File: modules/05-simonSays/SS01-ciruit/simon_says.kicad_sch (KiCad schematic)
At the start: 18 parts, among them J1 MODULE Connector

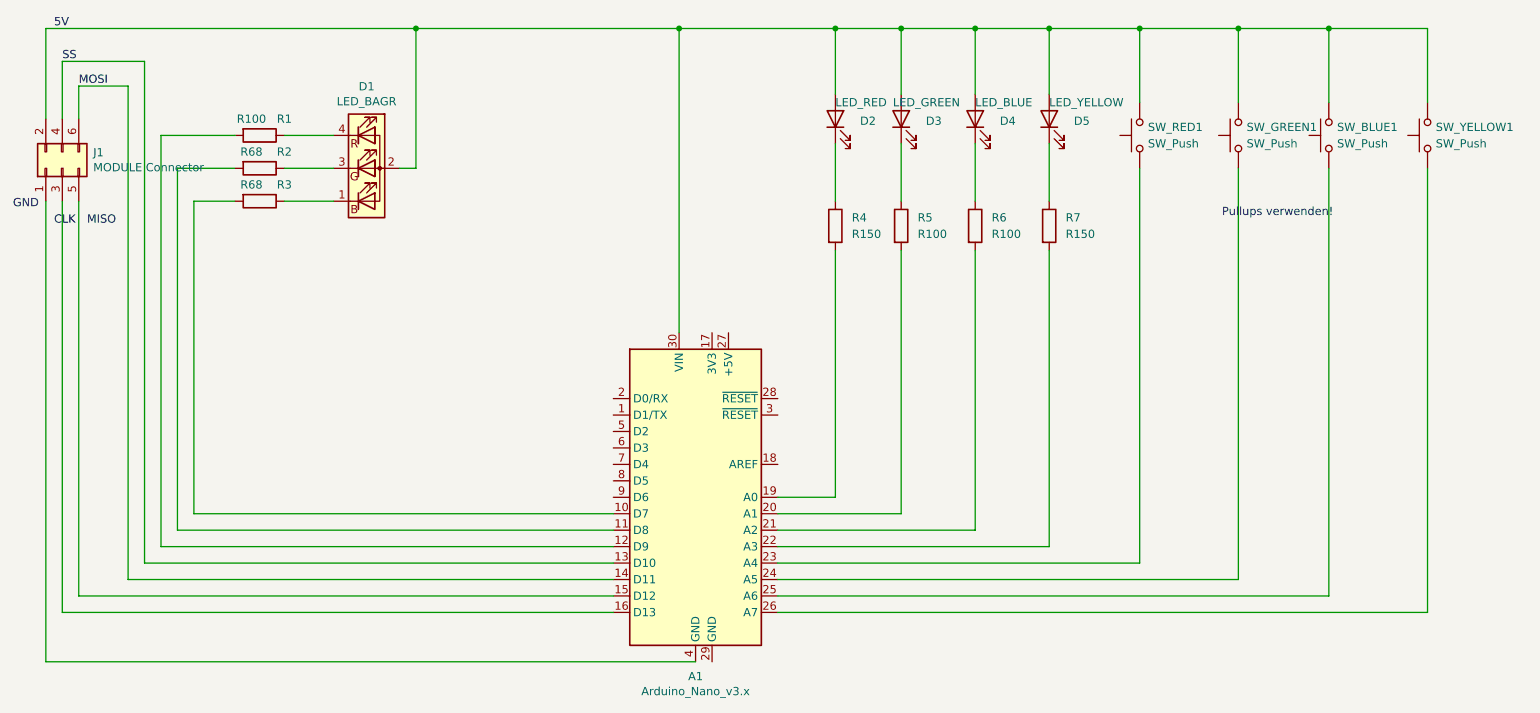
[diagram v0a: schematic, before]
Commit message: cleanup circuit
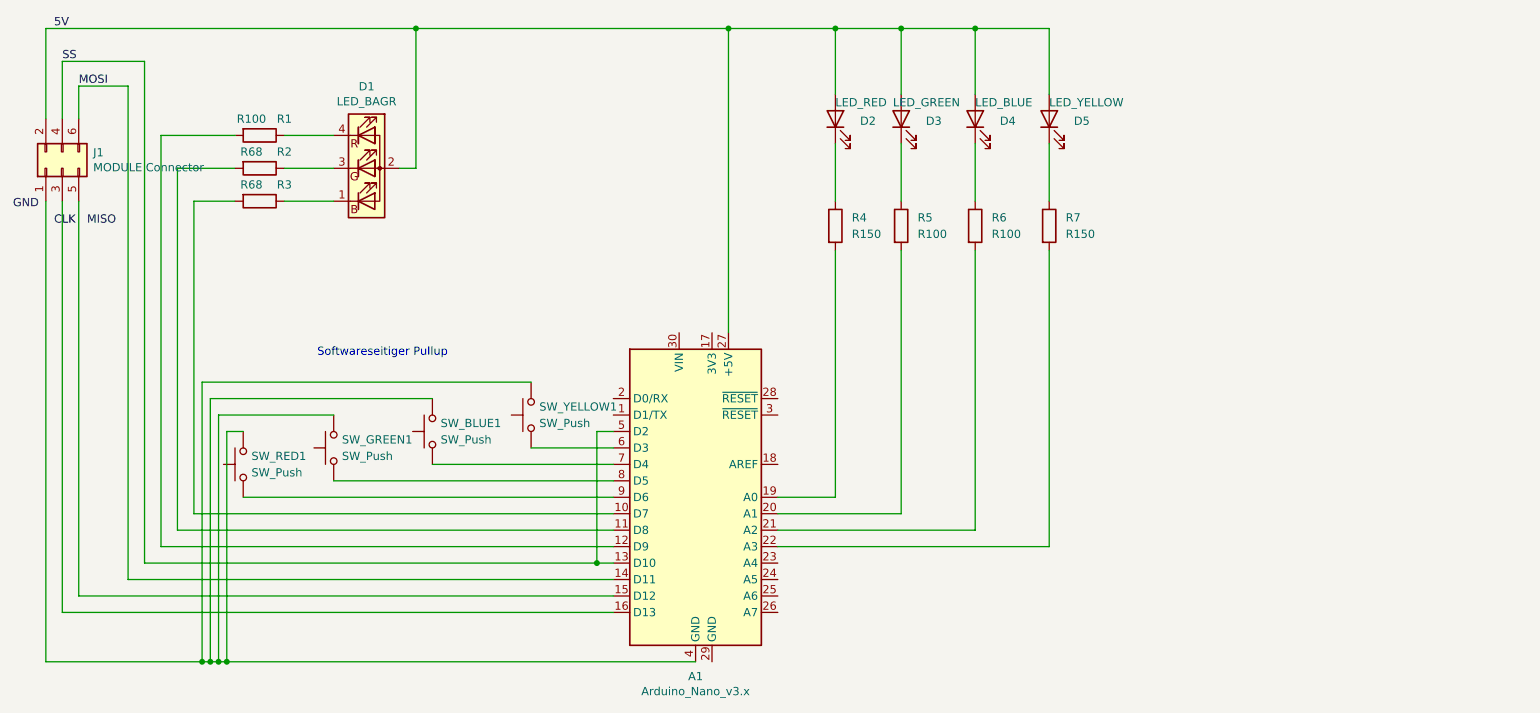
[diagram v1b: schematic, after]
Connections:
- net 5V: now also A1.27 (+5V); no longer A1.30 (VIN), SW_BLUE1.2, SW_GREEN1.2, SW_RED1.2, SW_YELLOW1.2
- net SS: now also A1.5 (D2)
- net at A1.4 (GND), J1.1 (Pin_1): now also SW_BLUE1.2, SW_GREEN1.2, SW_RED1.2, SW_YELLOW1.2
- net at A1.23 (A4): no longer SW_RED1.1
- net at A1.24 (A5): no longer SW_GREEN1.1
- net at A1.25 (A6): no longer SW_BLUE1.1
- net at A1.26 (A7): no longer SW_YELLOW1.1
- net at A1.6 (D3): now also SW_YELLOW1.1
- net at A1.7 (D4): now also SW_BLUE1.1
- net at A1.8 (D5): now also SW_GREEN1.1
- net at A1.9 (D6): now also SW_RED1.1
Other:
- note added: "Softwareseitiger Pullup"
- note removed: "Pullups verwenden!"
- title: (none) -> Schaltplan Modul SimonSays (05)
- moved on the sheet: SW_BLUE1, SW_GREEN1, SW_RED1, SW_YELLOW1
